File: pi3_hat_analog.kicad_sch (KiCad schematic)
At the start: 48 parts, among them J1 1935161, J3 Raspberry_Pi_2_3, J4 SJ1-3533NG, J5 SJ1-3533NG, J6 SJ1-3533NG, J7 SJ1-3533NG, Q1 2N3904BU, U1 MAX31856, U2 MCP3564RT, U3 MAX31856

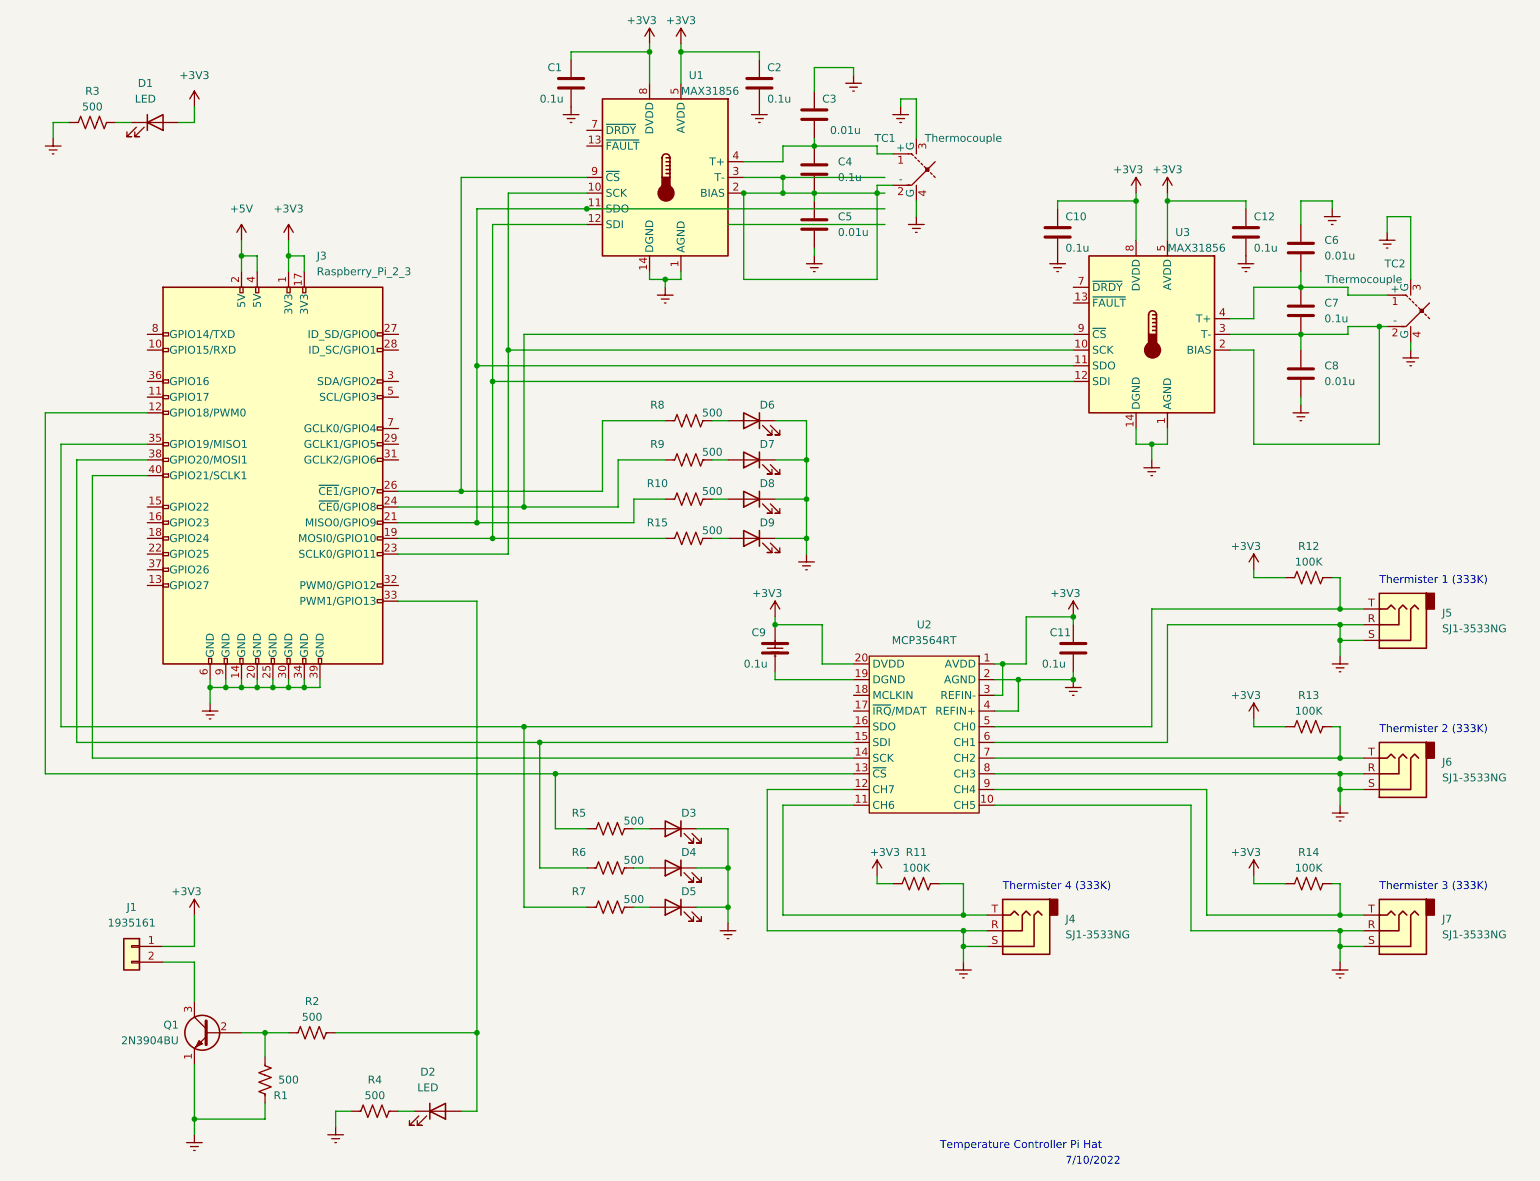
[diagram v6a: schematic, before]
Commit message: initial component placement complete
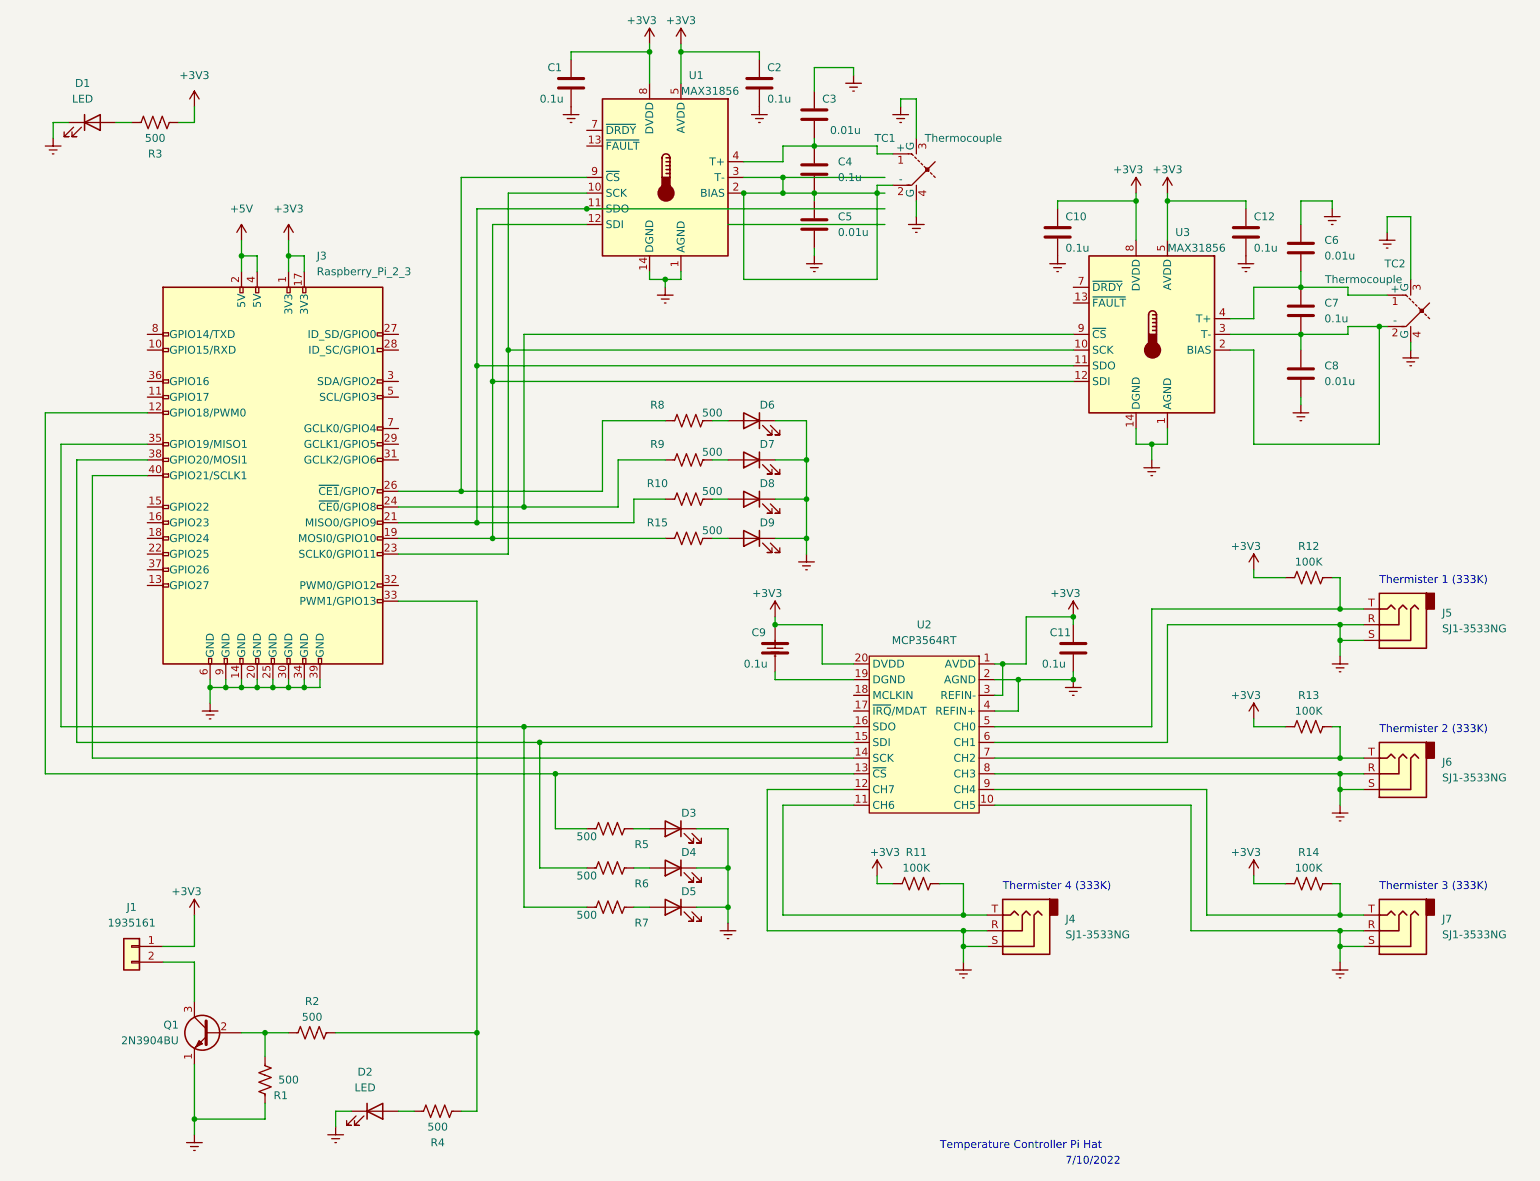
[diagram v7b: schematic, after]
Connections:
- net +3V3: now also R3.1; no longer D1.2 (A)
- net GNDREF: now also D1.1 (K), D2.1 (K); no longer R3.1, R4.1
- net at D3.2 (A): now also R5.1; no longer R5.2
- net at R3.2: now also D1.2 (A); no longer D1.1 (K)
- net at J3.12 (GPIO18/PWM0), U2.13 (~{CS}): now also R5.2; no longer R5.1
- net at J3.33 (PWM1/GPIO13), R2.2: now also R4.1; no longer D2.2 (A)
- net at J3.35 (GPIO19/MISO1), U2.16 (SDO): now also R7.2; no longer R7.1
- net at J3.38 (GPIO20/MOSI1), U2.15 (SDI): now also R6.2; no longer R6.1
- net at D4.2 (A): now also R6.1; no longer R6.2
- net at R4.2: now also D2.2 (A); no longer D2.1 (K)
- net at D5.2 (A): now also R7.1; no longer R7.2
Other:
- moved on the sheet: D1, D2, R3, R4, R5, R6, R7
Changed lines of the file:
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@@
     (stroke (width 0) (type default) (color 0 0 0 0))
   )
-  (wire (pts (xy 82.55 190.5) (xy 85.09 190.5))
+  (wire (pts (xy 85.09 190.5) (xy 82.55 190.5))
     (stroke (width 0) (type default) (color 0 0 0 0))
   )
@@
     (stroke (width 0) (type default) (color 0 0 0 0))
   )
-  (wire (pts (xy 36.83 30.48) (xy 39.37 30.48))
+  (wire (pts (xy 39.37 30.48) (xy 36.83 30.48))
     (stroke (width 0) (type default) (color 0 0 0 0))
   )
@@
     (pin "2")
   )
-  (symbol (lib_id "Device:LED") (at 43.18 30.48 0) (unit 1)
-    (in_bom yes) (on_board yes) (fields_autoplaced)
-    (property "Reference" "D1" (id 0) (at 41.5925 24.13 0))
-    (property "Value" "LED" (id 1) (at 41.5925 26.67 0))
-    (property "Footprint" "LED_SMD:LED_0603_1608Metric_Pad1.05x0.95mm_HandSolder" (id 2) (at 43.18 30.48 0)
-      (effects (font (size 1.27 1.27)) hide)
-    )
-    (property "Datasheet" "~" (id 3) (at 43.18 30.48 0)
+  (symbol (lib_id "Device:LED") (at 33.02 30.48 0) (unit 1)
+    (in_bom yes) (on_board yes) (fields_autoplaced)
+    (property "Reference" "D1" (id 0) (at 31.4325 24.13 0))
+    (property "Value" "LED" (id 1) (at 31.4325 26.67 0))
+    (property "Footprint" "LED_SMD:LED_0603_1608Metric_Pad1.05x0.95mm_HandSolder" (id 2) (at 33.02 30.48 0)
+      (effects (font (size 1.27 1.27)) hide)
+    )
+    (property "Datasheet" "~" (id 3) (at 33.02 30.48 0)
       (effects (font (size 1.27 1.27)) hide)
     )
@@
     (pin "1")
   )
-  (symbol (lib_id "Device:R_US") (at 116.84 151.13 90) (unit 1)
-    (in_bom yes) (on_board yes)
-    (property "Reference" "R6" (id 0) (at 111.76 148.59 90))
-    (property "Value" "500" (id 1) (at 120.65 149.86 90))
-    (property "Footprint" "Resistor_SMD:R_0603_1608Metric_Pad0.98x0.95mm_HandSolder" (id 2) (at 117.094 150.114 90)
+  (symbol (lib_id "Device:R_US") (at 116.84 151.13 270) (unit 1)
+    (in_bom yes) (on_board yes)
+    (property "Reference" "R6" (id 0) (at 121.92 153.67 90))
+    (property "Value" "500" (id 1) (at 113.03 152.4 90))
+    (property "Footprint" "Resistor_SMD:R_0603_1608Metric_Pad0.98x0.95mm_HandSolder" (id 2) (at 116.586 152.146 90)
       (effects (font (size 1.27 1.27)) hide)
     )
@@
     (pin "2")
   )
-  (symbol (lib_id "Device:R_US") (at 33.02 30.48 90) (unit 1)
-    (in_bom yes) (on_board yes)
-    (property "Reference" "R3" (id 0) (at 33.02 25.4 90))
-    (property "Value" "500" (id 1) (at 33.02 27.94 90))
-    (property "Footprint" "Resistor_SMD:R_0603_1608Metric_Pad0.98x0.95mm_HandSolder" (id 2) (at 33.274 29.464 90)
-      (effects (font (size 1.27 1.27)) hide)
-    )
-    (property "Datasheet" "~" (id 3) (at 33.02 30.48 0)
+  (symbol (lib_id "Device:R_US") (at 43.18 30.48 270) (unit 1)
+    (in_bom yes) (on_board yes)
+    (property "Reference" "R3" (id 0) (at 43.18 35.56 90))
+    (property "Value" "500" (id 1) (at 43.18 33.02 90))
+    (property "Footprint" "Resistor_SMD:R_0603_1608Metric_Pad0.98x0.95mm_HandSolder" (id 2) (at 42.926 31.496 90)
+      (effects (font (size 1.27 1.27)) hide)
+    )
+    (property "Datasheet" "~" (id 3) (at 43.18 30.48 0)
       (effects (font (size 1.27 1.27)) hide)
     )
@@
     (pin "2")
   )
-  (symbol (lib_id "Device:LED") (at 88.9 190.5 0) (unit 1)
-    (in_bom yes) (on_board yes) (fields_autoplaced)
-    (property "Reference" "D2" (id 0) (at 87.3125 184.15 0))
-    (property "Value" "LED" (id 1) (at 87.3125 186.69 0))
-    (property "Footprint" "LED_SMD:LED_0603_1608Metric_Pad1.05x0.95mm_HandSolder" (id 2) (at 88.9 190.5 0)
+  (symbol (lib_id "Device:LED") (at 78.74 190.5 0) (unit 1)
+    (in_bom yes) (on_board yes) (fields_autoplaced)
+    (property "Reference" "D2" (id 0) (at 77.1525 184.15 0))
+    (property "Value" "LED" (id 1) (at 77.1525 186.69 0))
+    (property "Footprint" "LED_SMD:LED_0603_1608Metric_Pad1.05x0.95mm_HandSolder" (id 2) (at 78.74 190.5 0)
+      (effects (font (size 1.27 1.27)) hide)
+    )
+    (property "Datasheet" "~" (id 3) (at 78.74 190.5 0)
+      (effects (font (size 1.27 1.27)) hide)
+    )
+    (pin "1")
+    (pin "2")
+  )
+  (symbol (lib_id "Device:R_US") (at 88.9 190.5 270) (unit 1)
+    (in_bom yes) (on_board yes)
+    (property "Reference" "R4" (id 0) (at 88.9 195.58 90))
+    (property "Value" "500" (id 1) (at 88.9 193.04 90))
+    (property "Footprint" "Resistor_SMD:R_0603_1608Metric_Pad0.98x0.95mm_HandSolder" (id 2) (at 88.646 191.516 90)
       (effects (font (size 1.27 1.27)) hide)
     )
@@
     (pin "2")
   )
-  (symbol (lib_id "Device:R_US") (at 78.74 190.5 90) (unit 1)
-    (in_bom yes) (on_board yes)
-    (property "Reference" "R4" (id 0) (at 78.74 185.42 90))
-    (property "Value" "500" (id 1) (at 78.74 187.96 90))
-    (property "Footprint" "Resistor_SMD:R_0603_1608Metric_Pad0.98x0.95mm_HandSolder" (id 2) (at 78.994 189.484 90)
-      (effects (font (size 1.27 1.27)) hide)
-    )
-    (property "Datasheet" "~" (id 3) (at 78.74 190.5 0)
-      (effects (font (size 1.27 1.27)) hide)
-    )
-    (pin "1")
-    (pin "2")
-  )
   (symbol (lib_name "GNDREF_14") (lib_id "power:GNDREF") (at 49.53 194.31 0) (unit 1)
     (in_bom yes) (on_board yes) (fields_autoplaced)
@@
     (pin "1")
   )
-  (symbol (lib_id "Device:R_US") (at 116.84 157.48 90) (unit 1)
-    (in_bom yes) (on_board yes)
-    (property "Reference" "R7" (id 0) (at 111.76 154.94 90))
-    (property "Value" "500" (id 1) (at 120.65 156.21 90))
-    (property "Footprint" "Resistor_SMD:R_0603_1608Metric_Pad0.98x0.95mm_HandSolder" (id 2) (at 117.094 156.464 90)
+  (symbol (lib_id "Device:R_US") (at 116.84 157.48 270) (unit 1)
+    (in_bom yes) (on_board yes)
+    (property "Reference" "R7" (id 0) (at 121.92 160.02 90))
+    (property "Value" "500" (id 1) (at 113.03 158.75 90))
+    (property "Footprint" "Resistor_SMD:R_0603_1608Metric_Pad0.98x0.95mm_HandSolder" (id 2) (at 116.586 158.496 90)
       (effects (font (size 1.27 1.27)) hide)
     )
@@
     (pin "1")
   )
-  (symbol (lib_id "Device:R_US") (at 116.84 144.78 90) (unit 1)
-    (in_bom yes) (on_board yes)
-    (property "Reference" "R5" (id 0) (at 111.76 142.24 90))
-    (property "Value" "500" (id 1) (at 120.65 143.51 90))
-    (property "Footprint" "Resistor_SMD:R_0603_1608Metric_Pad0.98x0.95mm_HandSolder" (id 2) (at 117.094 143.764 90)
-      (effects (font (size 1.27 1.27)) hide)
-    )
+  (symbol (lib_id "Device:R_US") (at 116.84 144.78 270) (unit 1)
+    (in_bom yes) (on_board yes)
+    (property "Reference" "R5" (id 0) (at 121.92 147.32 90))
+    (property "Value" "500" (id 1) (at 113.03 146.05 90))
+    (property "Footprint" "Resistor_SMD:R_0603_1608Metric_Pad0.98x0.95mm_HandSolder" (id 2) (at 116.586 145.796 90)
+      (effects (font (size 1.27 1.27)) hide)
+    )
